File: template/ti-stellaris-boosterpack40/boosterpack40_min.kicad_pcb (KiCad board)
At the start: 2 copper layers, 4 parts, among them J1 TI_BOOSTER_40_J1, J2 TI_BOOSTER_40_J2, J3 TI_BOOSTER_40_J3, J4 TI_BOOSTER_40_J4

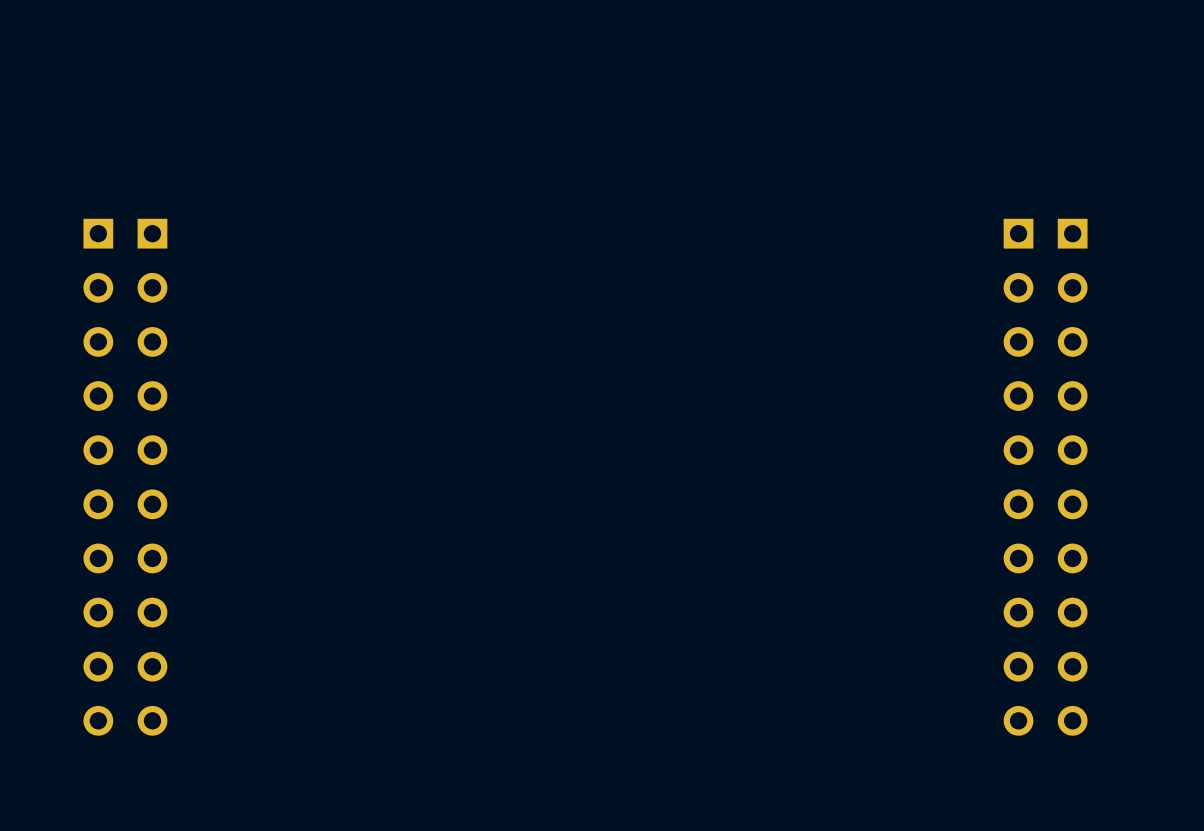
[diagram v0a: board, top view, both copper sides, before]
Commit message: fix #252: template layers translated
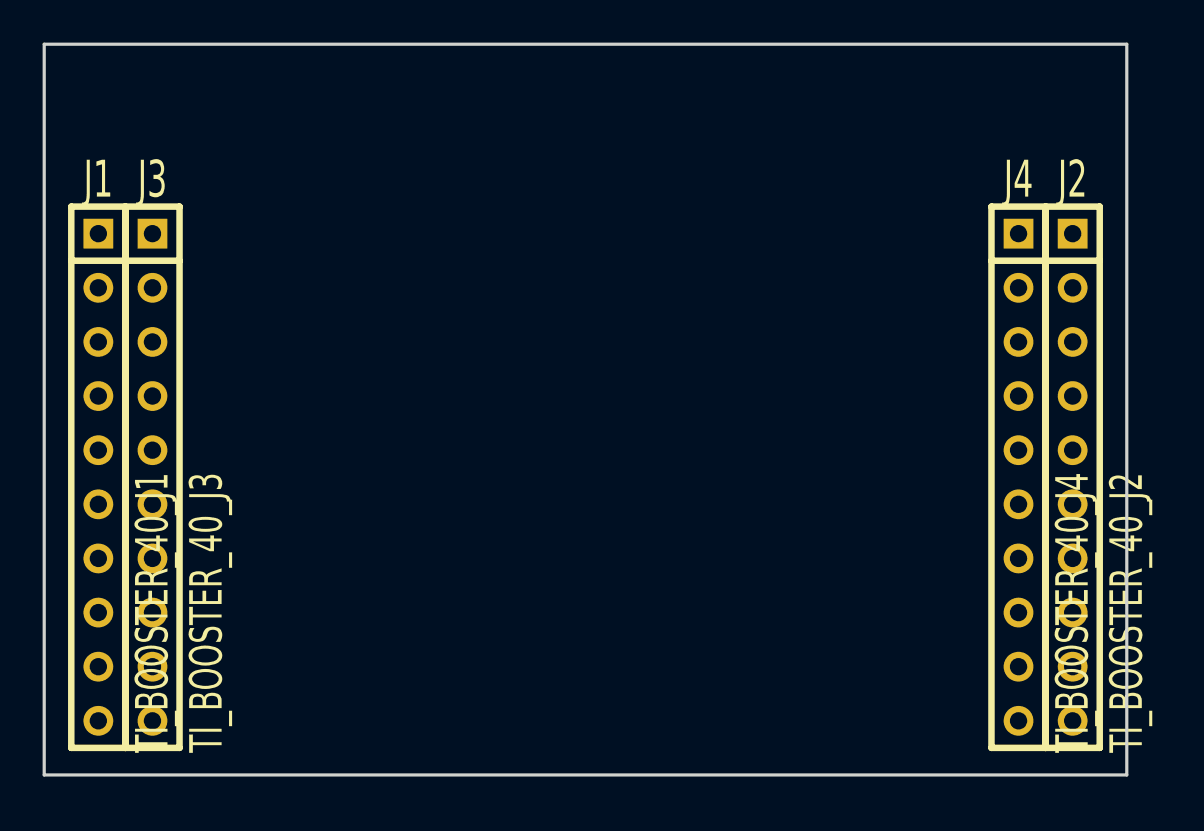
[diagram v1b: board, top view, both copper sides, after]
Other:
- board outline added: 50.8 x 34.3 mm
